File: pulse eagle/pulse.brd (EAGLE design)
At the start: 21 x 31.1 mm, 25 parts, among them IC1 LM358D, J1 ISP Touch, T1 MMBT3904, Y1 8MHz

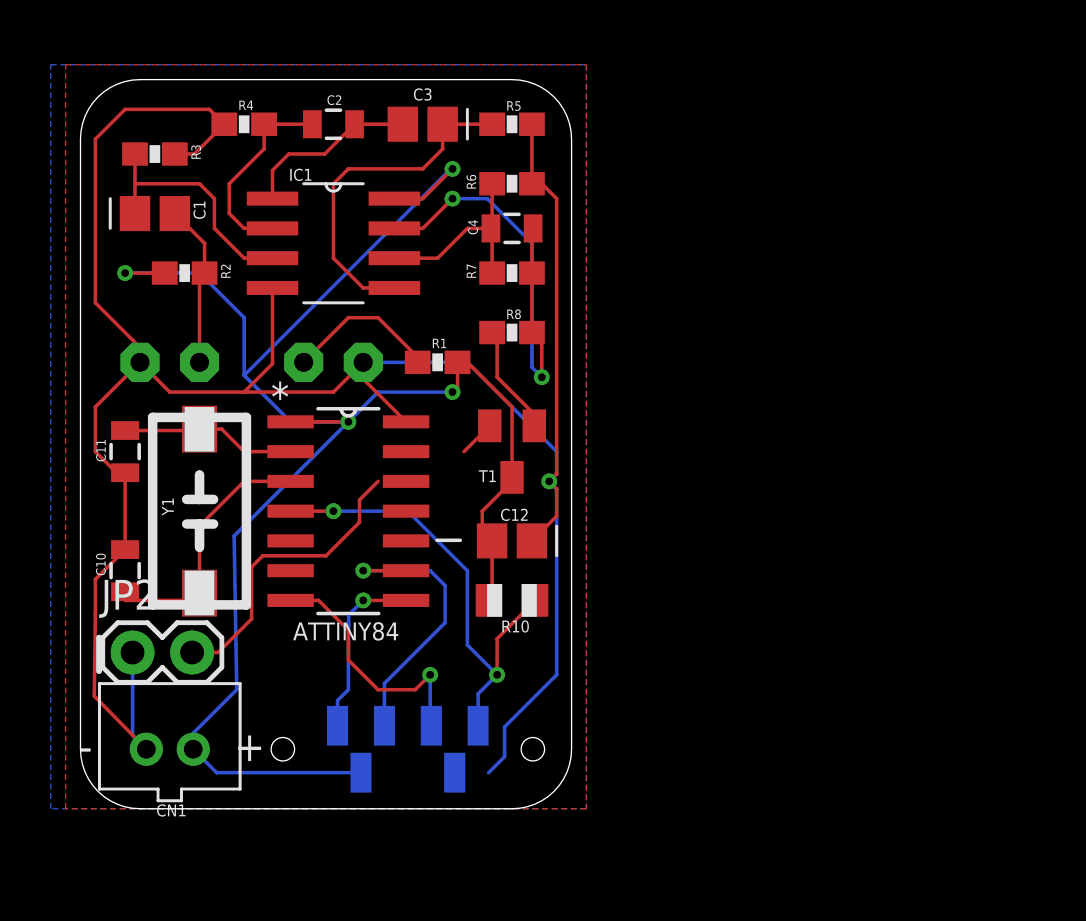
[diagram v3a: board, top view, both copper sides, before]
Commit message: Rev. 2 of the board, with new headers for el wire, led data, and pwm led.
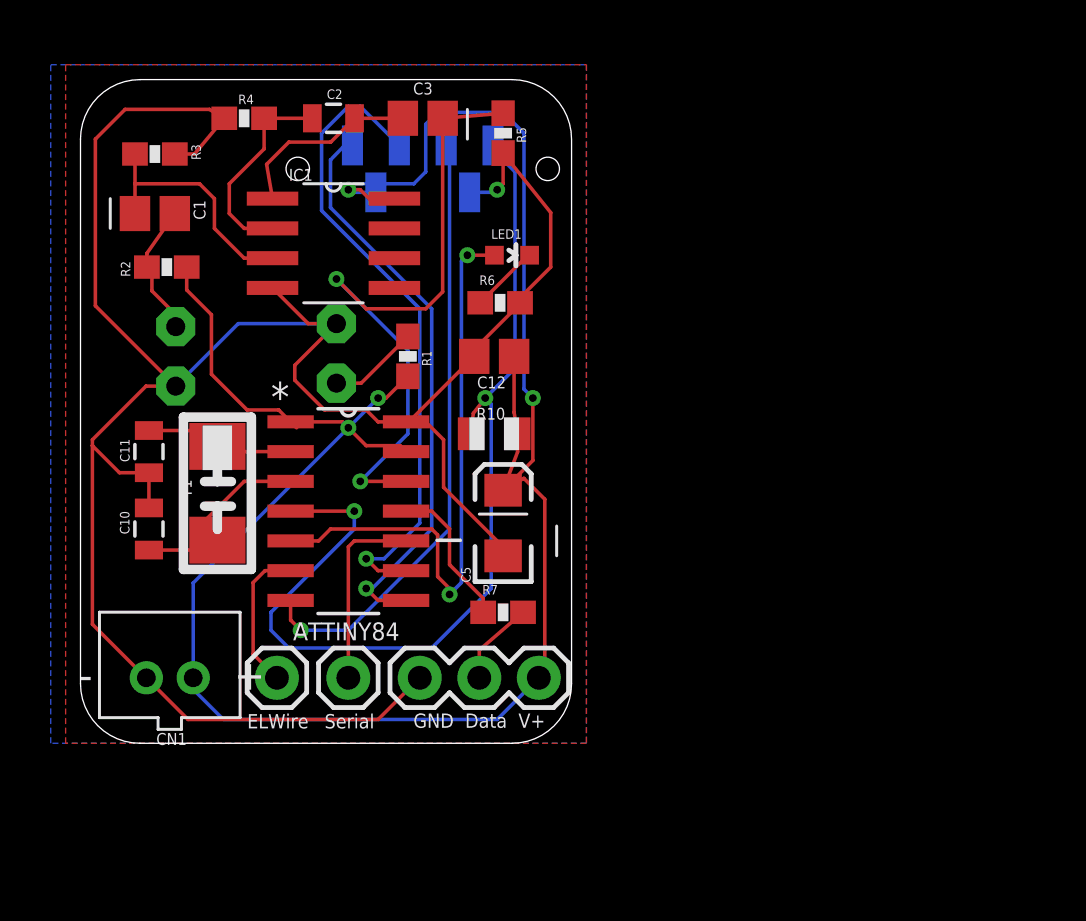
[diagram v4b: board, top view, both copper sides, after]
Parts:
- removed C4: .1uF, SparkFun-Passives:0805
- removed R8: 1.8k, SparkFun-Resistors:0603-RES
- removed T1: MMBT3904, transistor:SOT23
- added C5: 100uF, SparkFun-Capacitors:EIA3216
- added JP3: ELWire, SparkFun-Connectors:1X01
- added JP4: (no value), SparkFun-Connectors:1X03
- added LED1: (no value), SparkFun-LED:LED-0603
- C10, C11: value 15pF -> 8pF
- JP2: value M02PTH -> Serial; device SparkFun-Connectors:1X02 -> SparkFun-Connectors:1X01
- R6: value 1k -> 1.5k
- R7: value 470k -> 220
- Y1: device remote:NX8045GB -> remote:NX5032GA
- moved J1 24.8 mm to (14.6, 27.3)
- moved R7 14.5 mm to (18.0, 8.38), turned to 0 degrees
- moved JP2 9.27 mm to (11.4, 5.59)
- moved C12 7.91 mm to (17.7, 19.3), turned to 180 degrees
- moved R10 7.15 mm to (17.7, 16.0), turned to 180 degrees
- moved R6 5.11 mm to (17.9, 21.6), turned to 0 degrees
- moved CN1 3.05 mm to (3.81, 5.59)
- moved C10 2.05 mm to (2.92, 11.9)
- moved R1 1.30 mm to (14.0, 19.3), turned to 270 degrees
- moved Y1 1.08 mm to (5.84, 13.5)
- moved C11 1.02 mm to (2.92, 15.2)
- moved R2 0.80 mm to (3.68, 23.1), turned to 0 degrees
- moved R5 0.54 mm to (18.0, 28.8), turned to 90 degrees
- moved IR_EMIT 0.40 mm to (10.9, 19.4), turned to 90 degrees
- moved IR_REC 0.36 mm to (4.06, 19.3), turned to 270 degrees
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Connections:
- removed net N$6: C3.2, IC1.5, R5.2
- removed net N$9: R8.1, T1.1
- new net BEATLED: ATTINY84.11, R7.1
- new net ELWIRE: ATTINY84.6, JP3.1
- new net REALLED: ATTINY84.5, LED1.A
- net A0: now also C3.2, R5.2; no longer T1.2
- net GND: now also C5.C, JP4.1, R6.2; no longer JP2.1, R6.1
- net N$7: now also JP4.2; no longer C4.1, IC1.6, R6.2
- net N$8: now also LED1.C, R6.1; no longer C4.2, IC1.7, R7.1, R8.2
- net SERIAL: now also ATTINY84.10, JP2.1; no longer ATTINY84.11, JP2.2
- net VCC: now also C5.A, JP4.3; no longer T1.3
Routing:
- net A0: track 1.56 -> 28.0 mm, vias 0 -> 2
- net REALLED: track 0.00 -> 25.3 mm, vias 0 -> 2
- net RESET: track 19.9 -> 41.7 mm
- net VCC: track 76.1 -> 94.5 mm
- net MISO: track 7.63 -> 25.2 mm
- net N$8: track 19.6 -> 2.93 mm, vias 2 -> 0
- net MOSI: track 10.7 -> 26.0 mm
- net SCK: track 12.6 -> 27.7 mm
- net N$6: track 14.7 -> 0.00 mm
- net GND: track 106.1 -> 99.6 mm
- net BEATLED: track 0.00 -> 6.32 mm
- net ELWIRE: track 0.00 -> 6.30 mm
- net N$9: track 5.08 -> 0.00 mm
- net N$7: track 8.50 -> 3.65 mm
- net SERIAL: track 12.8 -> 8.16 mm
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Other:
- board size 21 x 31.1 mm -> 21 x 28.3 mm
- board text added: "GND Data V+"
- board text added: "Pulse & Bloom 9 June 2014 - Rev. 2"
- board text removed: "Pulse & Bloom 9 May 2014 - Rev. A"

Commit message: Switching from attiny84 to atmega328 for the hardware serial, bigger flash size, additional PWMs, and negligible package size difference.
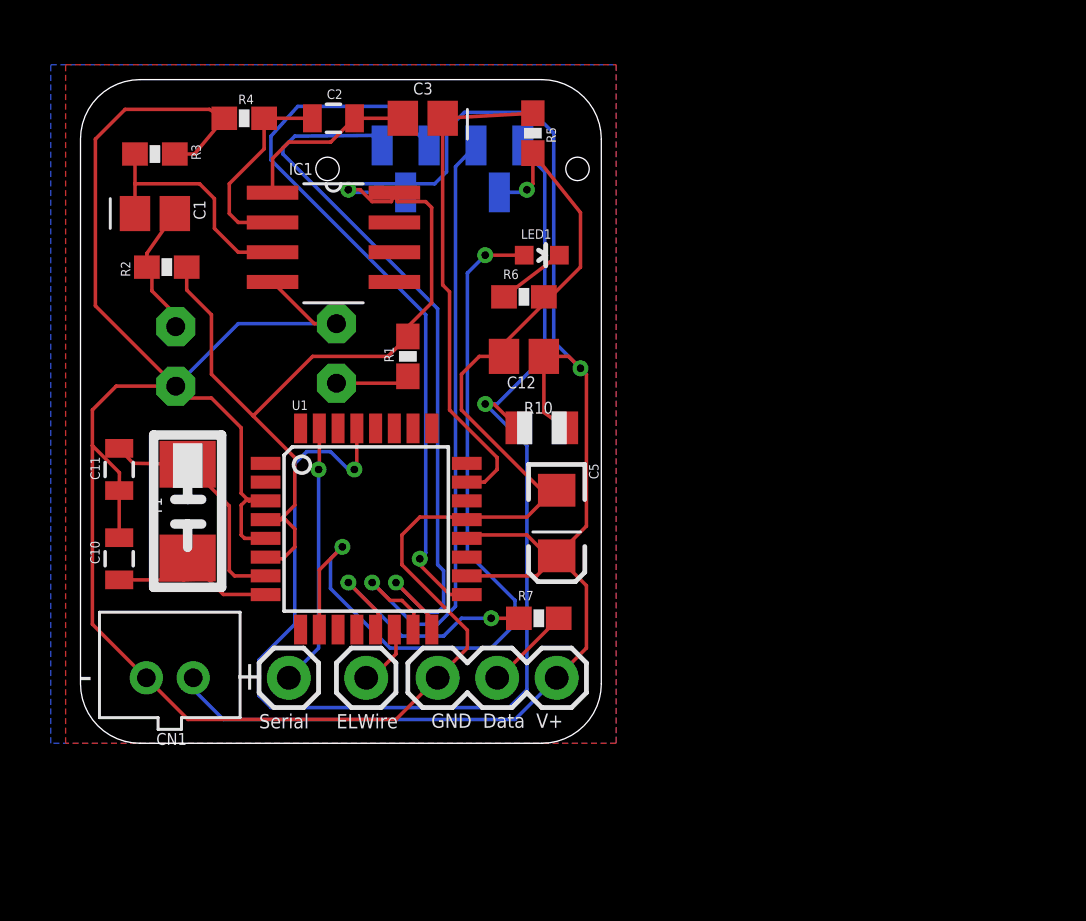
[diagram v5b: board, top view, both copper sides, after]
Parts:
- removed ATTINY84: (no value), Atmel_By_element14_Batch_1:SOIC127P600X175-14N
- added U1: ATMEGA328P, SparkFun-DigitalIC:TQFP32-08
- moved JP3 3.81 mm to (12.2, 5.59)
- moved JP2 2.54 mm to (8.89, 5.59)
- moved C5 2.29 mm to (20.3, 12.2), turned to 270 degrees
- moved R10 2.05 mm to (19.7, 16.3)
- moved C10 1.80 mm to (1.65, 10.7)
- moved R7 1.55 mm to (19.6, 8.13)
- moved C11 1.48 mm to (1.65, 14.5)
- moved Y1 1.48 mm to (4.57, 12.7)
- moved C12 1.27 mm to (18.9, 19.3)
- moved J1 1.27 mm to (15.9, 27.3)
- moved LED1 1.27 mm to (19.7, 23.6)
- moved R5 1.27 mm to (19.3, 28.8)
- moved R6 1.05 mm to (18.9, 21.8)
- moved JP4 0.76 mm to (15.2, 5.59)
- moved IC1 0.25 mm to (10.8, 24.4)
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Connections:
- removed net REALLED: ATTINY84.5, LED1.A
- new net STEMLED: R7.1, U1.13
- net A0: now also U1.23; no longer ATTINY84.12
- net BEATLED: now also LED1.A, U1.10; no longer ATTINY84.11, R7.1
- net ELWIRE: now also U1.14; no longer ATTINY84.6
- net GND: now also U1.21, U1.3, U1.5; no longer ATTINY84.14
- net MISO: now also U1.16; no longer ATTINY84.8
- net MOSI: now also U1.15; no longer ATTINY84.7
- net RESET: now also U1.29; no longer ATTINY84.4
- net SCK: now also U1.17; no longer ATTINY84.9
- net SERIAL: now also U1.31; no longer ATTINY84.10
- net VCC: now also U1.18, U1.20, U1.4, U1.6; no longer ATTINY84.1, ATTINY84.13
- net XTL1: now also U1.7; no longer ATTINY84.2
- net XTL2: now also U1.8; no longer ATTINY84.3
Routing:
- net BEATLED: track 6.32 -> 33.8 mm, vias 0 -> 2
- net REALLED: track 25.3 -> 0.00 mm, vias 2 -> 0
- net GND: track 99.6 -> 116.5 mm
- net RESET: track 41.7 -> 54.9 mm
- net VCC: track 94.5 -> 107.5 mm, vias 4 -> 2
- net STEMLED: track 0.00 -> 11.1 mm, vias 0 -> 2
- net MISO: track 25.2 -> 32.3 mm
- net A0: track 28.0 -> 21.3 mm, vias 2 -> 0
- net SCK: track 27.7 -> 31.7 mm
- net ELWIRE: track 6.30 -> 2.76 mm
- net SERIAL: track 8.16 -> 11.2 mm, vias 0 -> 1
- net XTL1: track 7.22 -> 10.1 mm
- net MOSI: track 26.0 -> 27.7 mm
- net XTL2: track 8.78 -> 7.48 mm
- net N$1: track 3.87 -> 3.20 mm
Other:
- board size 21 x 28.3 mm -> 22.2 x 28.3 mm
- board text added: "Pulse & Bloom 10 June 2014 - Rev. 3"
- board text removed: "Pulse & Bloom 9 June 2014 - Rev. 2"

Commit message: Switch from crappy IR sensors to SI1143 IC.
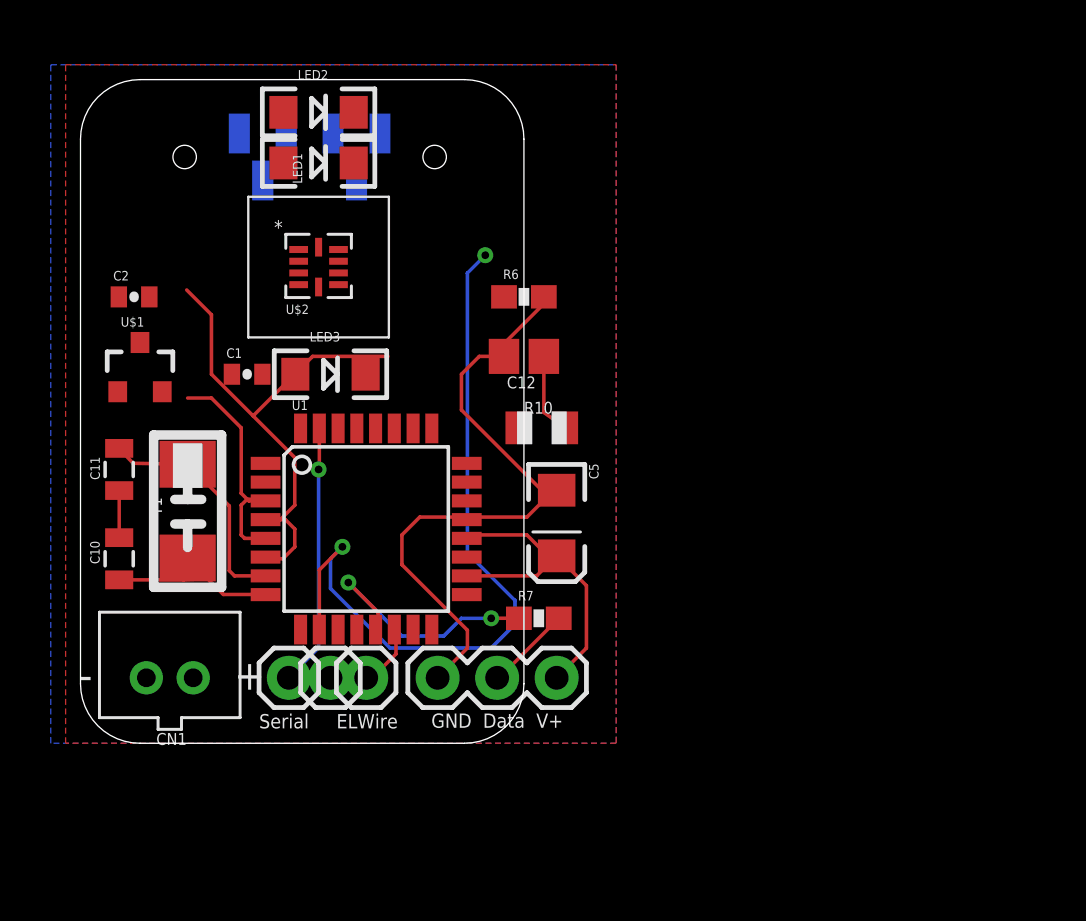
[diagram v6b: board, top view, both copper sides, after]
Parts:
- removed C3: 1uf, adafruit:C0805
- removed IC1: LM358D, linear:SO08
- removed IR_EMIT, IR_REC: (no value), adafruit:LED5MM
- removed R1: 220, SparkFun-Resistors:0603-RES
- removed R2: 39k, SparkFun-Resistors:0603-RES
- removed R3, R5: 68k, SparkFun-Resistors:0603-RES
- removed R4: 8.2k, SparkFun-Resistors:0603-RES
- added JP1: Petal, SparkFun-Connectors:1X01
- added LED2, LED3: (no value), SparkFun-LED:LED-1206
- added U$1: LM3480IM4, SparkFun-PowerIC:SOT23-3
- added U$2: SI1143, pulse:SI1143
- C1: value 1uf -> 0.1uF; device adafruit:C0805 -> SparkFun-Capacitors:0402-CAP
- C2: value .1uF -> 0.1uF; device SparkFun-Passives:0805 -> SparkFun-Capacitors:0402-CAP
- LED1: device SparkFun-LED:LED-0603 -> SparkFun-LED:LED-1206
- moved C2 11.4 mm to (2.29, 21.8)
- moved LED1 10.3 mm to (10.2, 27.6), turned to 0 degrees
- moved C1 7.91 mm to (7.11, 18.5), turned to 0 degrees
- moved J1 6.12 mm to (9.78, 27.8)
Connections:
- removed net A0: C3.2, R5.2, U1.23
- removed net N$1: IR_EMIT.A, R1.1
- removed net N$3: C1.2, IC1.3, R3.2
- removed net N$4: C2.1, IC1.2, R4.2
- removed net N$5: C2.2, C3.1, IC1.1
- removed net N$8: LED1.C, R6.1
- new net 3V3: C2.2, U$1.1, U$2.3
- new net LED1: LED1.C, U$2.9
- new net LED2: LED2.C, U$2.6
- new net LED3: LED3.C, U$2.7
- new net SCL: U$2.2, U1.28
- new net SDA: U$2.1, U1.27
- net BEATLED: now also JP1.1; no longer LED1.A
- net GND: now also C1.2, C2.1, U$1.3, U$2.8; no longer IC1.4, IR_EMIT.K, IR_REC.K, R3.1, R4.1, R5.1, R6.2
- net N$2: now also LED1.A, LED2.A, LED3.A, R6.2; no longer IR_REC.A, R2.1
- net VCC: now also R6.1, U$1.2; no longer IC1.8, R1.2, R2.2
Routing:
- net GND: track 116.5 -> 39.9 mm, vias 1 -> 0
- net VCC: track 107.5 -> 41.3 mm, vias 2 -> 0
- net RESET: track 54.9 -> 0.00 mm, vias 2 -> 0
- net MISO: track 32.3 -> 0.00 mm, vias 1 -> 0
- net SCK: track 31.7 -> 0.00 mm, vias 1 -> 0
- net MOSI: track 27.7 -> 0.00 mm, vias 1 -> 0
- net A0: track 21.3 -> 0.00 mm
- net N$3: track 10.4 -> 0.00 mm
- net N$4: track 8.74 -> 0.00 mm
- net N$5: track 7.73 -> 0.00 mm
- net N$2: track 5.71 -> 0.00 mm
- net N$1: track 3.20 -> 0.00 mm
- net N$8: track 2.96 -> 0.00 mm
- net BEATLED: track 33.8 -> 32.2 mm
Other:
- board size 22.2 x 28.3 mm -> 18.9 x 28.3 mm

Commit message: Re-orienting and preparing board for layout.
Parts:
- moved C5 16.8 mm to (4.32, 7.11), turned to 0 degrees
- moved JP4 5.33 mm to (9.91, 5.59)
- moved JP3 4.88 mm to (16.0, 2.54)
- moved R6 4.50 mm to (14.6, 23.1)
- moved R10 3.66 mm to (16.6, 18.3)
- moved JP1 3.53 mm to (12.4, 2.54)
- moved C12 3.30 mm to (15.9, 20.6)
- moved CN1 3.05 mm to (3.81, 2.54)
- moved JP2 3.05 mm to (8.89, 2.54)
- moved R7 2.90 mm to (17.8, 5.84), turned to 270 degrees
- moved C2 2.84 mm to (5.08, 22.4)
- moved C1 1.48 mm to (6.35, 19.8)
- moved U1 1.02 mm to (12.2, 13.0)
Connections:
- new net INT0: U$2.4, U1.32
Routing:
- net VCC: track 41.3 -> 0.00 mm
- net BEATLED: track 32.2 -> 0.00 mm, vias 2 -> 0
- net GND: track 39.9 -> 14.2 mm
- net SERIAL: track 11.2 -> 0.00 mm, vias 1 -> 0
- net STEMLED: track 11.1 -> 0.00 mm, vias 2 -> 0
- net N$7: track 3.66 -> 0.00 mm
- net ELWIRE: track 2.76 -> 0.00 mm
- net XTL2: track 7.48 -> 8.48 mm
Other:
- board size 18.9 x 28.3 mm -> 18.9 x 31.1 mm
